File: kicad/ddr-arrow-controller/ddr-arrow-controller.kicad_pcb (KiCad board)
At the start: 2 copper layers, 50 parts

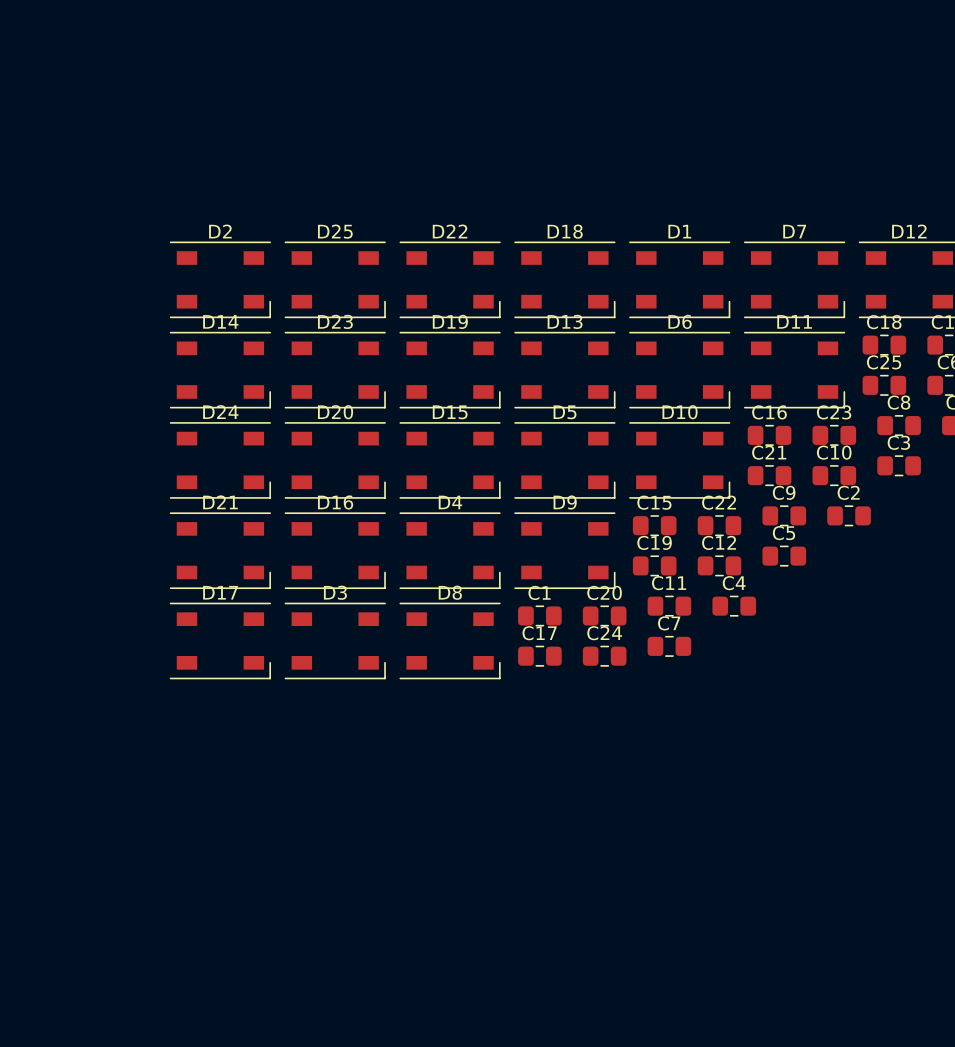
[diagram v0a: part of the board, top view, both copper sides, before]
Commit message: Schematic Updates
Placed microcontroller, CANBus chips, power regulator.
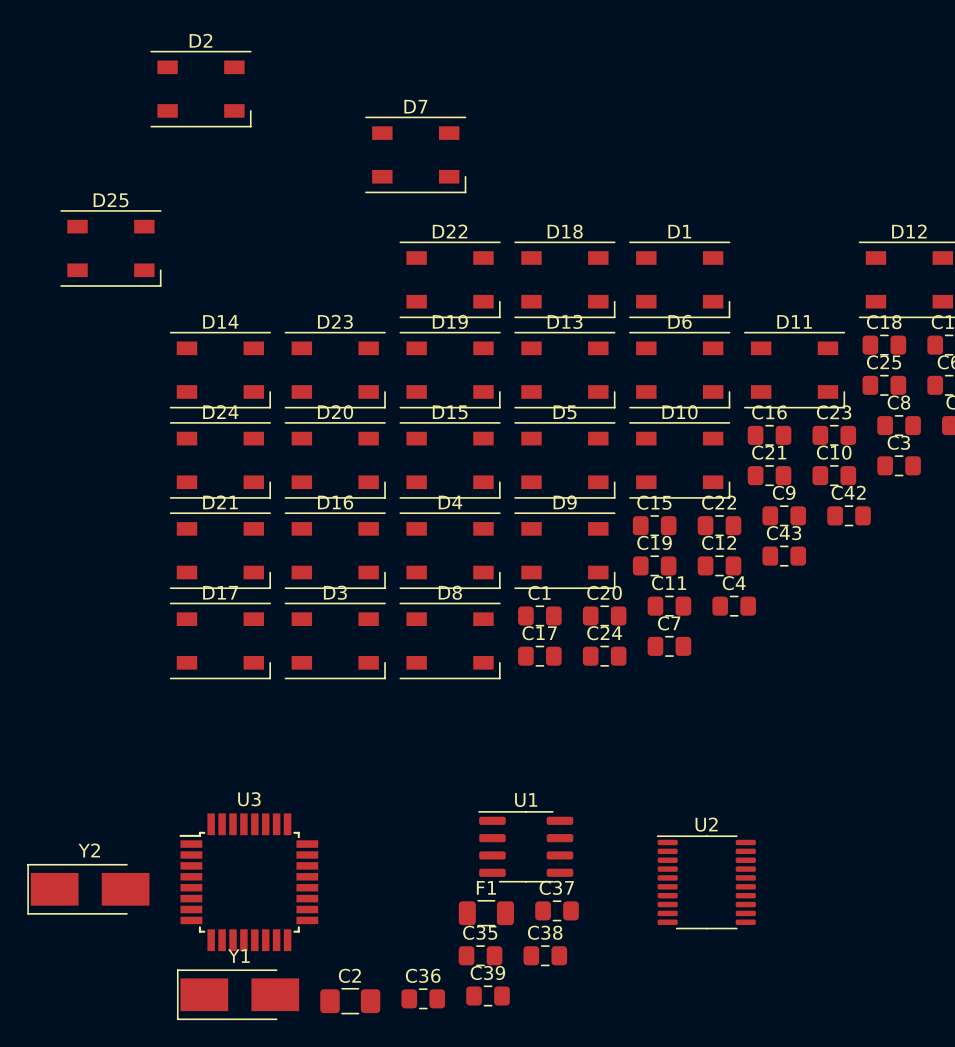
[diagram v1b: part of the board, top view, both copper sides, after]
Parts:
- added C2: 10uF, Capacitor_SMD:C_1206_3216Metric_Pad1.42x1.75mm_HandSolder, F.Cu at (36.3, 114.4)
- added C35: 1000uF, Capacitor_SMD:C_0805_2012Metric_Pad1.15x1.40mm_HandSolder, F.Cu at (45.9, 111.0)
- added C36: 1000uF, Capacitor_SMD:C_0805_2012Metric_Pad1.15x1.40mm_HandSolder, F.Cu at (41.7, 114.2)
- added C37: 1000uF, Capacitor_SMD:C_0805_2012Metric_Pad1.15x1.40mm_HandSolder, F.Cu at (51.5, 107.8)
- added C38: 1000uF, Capacitor_SMD:C_0805_2012Metric_Pad1.15x1.40mm_HandSolder, F.Cu at (50.6, 111.0)
- added C39: 1000uF, Capacitor_SMD:C_0805_2012Metric_Pad1.15x1.40mm_HandSolder, F.Cu at (46.4, 114.0)
- added F1: 1206L025YR, Fuse:Fuse_1206_3216Metric, F.Cu at (46.3, 107.9)
- added U1: TJA1051T, Package_SO:SOIC-8_3.9x4.9mm_P1.27mm, F.Cu at (49.2, 103.1)
- added U2: MCP2515-xST, Package_SO:TSSOP-20_4.4x6.5mm_P0.65mm, F.Cu at (62.5, 105.7)
- added U3: ATmega328PB-AU, Package_QFP:TQFP-32_7x7mm_P0.8mm, F.Cu at (28.9, 105.7)
- added Y1: 8MHz, Crystal:Crystal_SMD_5032-2Pin_5.0x3.2mm_HandSoldering, F.Cu at (28.2, 113.9)
- added Y2: 16MHz, Crystal:Crystal_SMD_5032-2Pin_5.0x3.2mm_HandSoldering, F.Cu at (17.3, 106.2)
- moved D7 29.2 mm to (41.1, 52.3)
- moved D25 16.6 mm to (18.8, 59.2)
- moved D2 14.1 mm to (25.4, 47.5)
- renumbered C2 to C42, C5 to C43
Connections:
- net +5V renamed VCC

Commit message: Board layout v1 complete
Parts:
- removed C36, C37, C38, C39: 1000uF, Capacitor_SMD:C_0805_2012Metric_Pad1.15x1.40mm_HandSolder
- added C26: 0.1uF, Capacitor_SMD:C_0805_2012Metric_Pad1.15x1.40mm_HandSolder, F.Cu at (152.9, 11.7)
- added C27: 0.022uF, Capacitor_SMD:C_0805_2012Metric_Pad1.15x1.40mm_HandSolder, F.Cu at (152.4, 20.3)
- added C28: 0.1uF, Capacitor_SMD:C_0805_2012Metric_Pad1.15x1.40mm_HandSolder, F.Cu at (105.2, 8.38)
- added C29: 10uF/16V, Capacitor_SMD:C_1206_3216Metric_Pad1.42x1.75mm_HandSolder, F.Cu at (105.7, 5.84)
- added C30: 22uF, Capacitor_SMD:C_0805_2012Metric_Pad1.15x1.40mm_HandSolder, F.Cu at (165.6, 21.3)
- added C31: 22uF, Capacitor_SMD:C_0805_2012Metric_Pad1.15x1.40mm_HandSolder, F.Cu at (151.9, 24.8)
- added C33: 22uF, Capacitor_SMD:C_0805_2012Metric_Pad1.15x1.40mm_HandSolder, F.Cu at (165.6, 23.9)
- added C34: 10uF, Capacitor_SMD:C_1206_3216Metric_Pad1.42x1.75mm_HandSolder, F.Cu at (165.1, 15.7)
- added C44: 0.1uF, Capacitor_SMD:C_0805_2012Metric_Pad1.15x1.40mm_HandSolder, F.Cu at (165.6, 18.8)
- added C5: 10uF/35V, Capacitor_SMD:C_1206_3216Metric_Pad1.42x1.75mm_HandSolder, F.Cu at (155.4, 11.2)
- added D26: RED, LED_SMD:LED_0805_2012Metric, F.Cu at (164.8, 40.6)
- added IC1: JanSquareLib_TS30013-M033QFNR, TS30013:QFN50P300X300X100-17N, F.Cu at (150.4, 16.3)
- added J10: OPTO, Connector_JST:JST_PH_B2B-PH-K_1x02_P2.00mm_Vertical, F.Cu at (21.8, 8.13)
- added J11: ST_POW, Connector_Molex:Molex_Mini-Fit_Jr_5569-02A2_2x01_P4.20mm_Horizontal, F.Cu at (142.7, 10.7)
- added J12: ST_CAN, TerminalBlock_Phoenix:TerminalBlock_Phoenix_MKDS-1,5-2_1x02_P5.00mm_Horizontal, F.Cu at (118.9, 5.46)
- added J13: Step Sensor, Connector_JST:JST_PH_B2B-PH-K_1x02_P2.00mm_Vertical, F.Cu at (8.64, 81.8)
- added J2: A0, Connector_JST:JST_PH_B2B-PH-K_1x02_P2.00mm_Vertical, F.Cu at (8.64, 89.0)
- added J3: A1, Connector_JST:JST_PH_B2B-PH-K_1x02_P2.00mm_Vertical, F.Cu at (162.6, 120.5)
- added J4: A2, Connector_JST:JST_PH_B2B-PH-K_1x02_P2.00mm_Vertical, F.Cu at (163.1, 51.3)
- added J5: A3, Connector_JST:JST_PH_B2B-PH-K_1x02_P2.00mm_Vertical, F.Cu at (31.2, 8.13)
- added J6: AVR-ISP-6, Connector_PinHeader_2.54mm:PinHeader_2x03_P2.54mm_Vertical, F.Cu at (73.4, 7.87)
- added JP1: LED_EN, Jumper:SolderJumper-2_P1.3mm_Bridged_Pad1.0x1.5mm, F.Cu at (157.5, 40.6)
- added JP2: Jumper_NO_Small, Connector_PinSocket_2.54mm:PinSocket_1x02_P2.54mm_Vertical, F.Cu at (113.5, 14.0)
- added L1: 4.7uH, Inductor_SMD:L_Taiyo-Yuden_NR-80xx_HandSoldering, F.Cu at (158.0, 20.3)
- added R1: 10K, Resistor_SMD:R_0805_2012Metric_Pad1.15x1.40mm_HandSolder, F.Cu at (68.4, 4.80)
- added R10: 10K, Resistor_SMD:R_0805_2012Metric_Pad1.15x1.40mm_HandSolder, F.Cu at (43.7, 34.5)
- added R11: 560, Resistor_SMD:R_0805_2012Metric_Pad1.15x1.40mm_HandSolder, F.Cu at (5.59, 71.6)
- added R12: 560, Resistor_SMD:R_0805_2012Metric_Pad1.15x1.40mm_HandSolder, F.Cu at (10.7, 71.6)
- added R13: 120, Resistor_SMD:R_0805_2012Metric_Pad1.15x1.40mm_HandSolder, F.Cu at (120.0, 14.1)
- added R2: 10K, Resistor_SMD:R_0805_2012Metric_Pad1.15x1.40mm_HandSolder, F.Cu at (105.2, 3.30)
- added R3: 560, Resistor_SMD:R_0805_2012Metric_Pad1.15x1.40mm_HandSolder, F.Cu at (18.3, 17.3)
- added R4: 1K, Resistor_SMD:R_0805_2012Metric_Pad1.15x1.40mm_HandSolder, F.Cu at (23.4, 17.3)
- added R5: 1K, Resistor_SMD:R_0805_2012Metric_Pad1.15x1.40mm_HandSolder, F.Cu at (161.0, 41.4)
- added R6: 10K, Resistor_SMD:R_0805_2012Metric_Pad1.15x1.40mm_HandSolder, F.Cu at (40.6, 34.5)
- added R7: 10K, Resistor_SMD:R_0805_2012Metric_Pad1.15x1.40mm_HandSolder, F.Cu at (38.1, 34.5)
- added R8: 10K, Resistor_SMD:R_0805_2012Metric_Pad1.15x1.40mm_HandSolder, F.Cu at (35.6, 34.5)
- added R9: 470, Resistor_SMD:R_0805_2012Metric_Pad1.15x1.40mm_HandSolder, F.Cu at (25.9, 21.3)
- added REF**: OSHW-Logo2_14.6x12mm_SilkScreen, Symbol:OSHW-Logo2_14.6x12mm_SilkScreen, F.Cu at (135.6, 159.3)
- added REF**: MountingHole_4.3mm_M4_DIN965_Pad, MountingHole:MountingHole_4.3mm_M4_DIN965_Pad, F.Cu at (166.0, 166.0)
- added REF**: MountingHole_4.3mm_M4_DIN965_Pad, MountingHole:MountingHole_4.3mm_M4_DIN965_Pad, F.Cu at (6.00, 166.0)
- added REF**: MountingHole_4.3mm_M4_DIN965_Pad, MountingHole:MountingHole_4.3mm_M4_DIN965_Pad, F.Cu at (6.00, 6.00)
- added REF**: MountingHole_4.3mm_M4_DIN965_Pad, MountingHole:MountingHole_4.3mm_M4_DIN965_Pad, F.Cu at (166.0, 6.00)
- added SW1: SW_Push, Button_Switch_SMD:SW_SPST_CK_RS282G05A3, F.Cu at (42.4, 6.86)
- added SW2: SW_DIP_x04, Button_Switch_SMD:SW_DIP_SPSTx04_Slide_9.78x12.34mm_W8.61mm_P2.54mm, F.Cu at (39.6, 43.7)
- added TP1: TP_PG, TestPoint:TestPoint_Pad_1.0x1.0mm, F.Cu at (148.5, 20.8)
- added TP10: PC5, TestPoint:TestPoint_Pad_1.0x1.0mm, B.Cu at (49.0, 11.7)
- added TP11: 5V, TestPoint:TestPoint_Pad_D2.0mm, B.Cu at (74.5, 18.2)
- added TP12: GND, TestPoint:TestPoint_Pad_D2.0mm, B.Cu at (71.5, 18.2)
- added TP13: PD0, TestPoint:TestPoint_Pad_D2.0mm, B.Cu at (65.3, 18.2)
- added TP14: PD1, TestPoint:TestPoint_Pad_D2.0mm, B.Cu at (68.4, 18.2)
- added TP2: TP_EN, TestPoint:TestPoint_Pad_1.0x1.0mm, F.Cu at (150.6, 22.0)
- added TP3: PE2, TestPoint:TestPoint_Pad_1.0x1.0mm, F.Cu at (72.4, 4.57)
- added TP4: PE3, TestPoint:TestPoint_Pad_1.0x1.0mm, F.Cu at (35.7, 3.40)
- added TP5: PB1, TestPoint:TestPoint_Pad_D2.0mm, F.Cu at (68.4, 16.6)
- added TP6: PB0, TestPoint:TestPoint_Pad_D2.0mm, F.Cu at (65.4, 16.6)
- added TP7: PE1, TestPoint:TestPoint_Pad_1.0x1.0mm, B.Cu at (64.2, 10.9)
- added TP8: PC4, TestPoint:TestPoint_Pad_1.0x1.0mm, B.Cu at (51.3, 11.6)
- added U4: TLP290, Package_SO:SOP-4_4.4x2.6mm_P1.27mm, F.Cu at (20.8, 14.2)
- added U5: TLP290, Package_SO:SOP-4_4.4x2.6mm_P1.27mm, F.Cu at (8.13, 75.2)
- C2: value 10uF -> 0.1uF; footprint Capacitor_SMD:C_1206_3216Metric_Pad1.42x1.75mm_HandSolder -> Capacitor_SMD:C_0805_2012Metric_Pad1.15x1.40mm_HandSolder
- C35: footprint Capacitor_SMD:C_0805_2012Metric_Pad1.15x1.40mm_HandSolder -> Capacitor_SMD:C_Elec_10x10.2
- U2: value MCP2515-xST -> MCP2515-xSO; footprint Package_SO:TSSOP-20_4.4x6.5mm_P0.65mm -> Package_SO:SOIC-18W_7.5x11.6mm_P1.27mm
- Y1: value 8MHz -> 16MHz; footprint Crystal:Crystal_SMD_5032-2Pin_5.0x3.2mm_HandSoldering -> Crystal:Resonator_SMD_muRata_CSTxExxV-3Pin_3.0x1.1mm_HandSoldering
- Y2: value 16MHz -> 8MHz; footprint Crystal:Crystal_SMD_5032-2Pin_5.0x3.2mm_HandSoldering -> Crystal:Resonator_SMD_muRata_CSTxExxV-3Pin_3.0x1.1mm_HandSoldering
- moved D25 153.7 mm to (145.8, 145.8), turned to 90 degrees
- moved C35 139.1 mm to (161.0, 33.0)
- moved Y2 129.0 mm to (99.6, 6.86), turned to 270 degrees
- moved D16 115.8 mm to (145.8, 115.8), turned to 270 degrees
- moved C2 115.3 mm to (63.2, 2.29), turned to 180 degrees
- moved D24 113.9 mm to (115.8, 145.8), turned to 90 degrees
- moved D5 105.7 mm to (145.9, 26.0), turned to 90 degrees
- moved C25 105.6 mm to (149.6, 144.4), turned to 270 degrees
- moved U1 104.6 mm to (105.2, 14.6)
- moved D15 102.7 mm to (145.8, 85.9), turned to 90 degrees
- moved U2 99.0 mm to (90.2, 10.7), turned to 180 degrees
- moved U3 98.9 mm to (56.4, 10.7), turned to 45 degrees
- moved Y1 98.6 mm to (52.3, 18.3), turned to 315 degrees
- moved C24 97.9 mm to (149.6, 114.4), turned to 270 degrees
- moved C21 97.3 mm to (149.9, 24.8), turned to 270 degrees
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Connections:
- C1 pad 1: VCC -> AVR_V
- C10 pad 1: VCC -> AVR_V
- C11 pad 1: VCC -> AVR_V
- C12 pad 1: VCC -> AVR_V
- C13 pad 1: VCC -> AVR_V
- C14 pad 1: VCC -> AVR_V
- C15 pad 1: VCC -> AVR_V
- C16 pad 1: VCC -> AVR_V
- C17 pad 1: VCC -> AVR_V
- C18 pad 1: VCC -> AVR_V
- C19 pad 1: VCC -> AVR_V
- C2 pad 1: VCC -> Net-(C2-Pad1)
- C20 pad 1: VCC -> AVR_V
- C21 pad 1: VCC -> AVR_V
- C22 pad 1: VCC -> AVR_V
- C23 pad 1: VCC -> AVR_V
- C24 pad 1: VCC -> AVR_V
- C25 pad 1: VCC -> AVR_V
- C3 pad 1: VCC -> AVR_V
- C35 pad 1: VCC -> AVR_V
- C4 pad 1: VCC -> AVR_V
- C42 pad 1: VCC -> AVR_V
- C43 pad 1: VCC -> AVR_V
- C6 pad 1: VCC -> AVR_V
- C7 pad 1: VCC -> AVR_V
- C8 pad 1: VCC -> AVR_V
- C9 pad 1: VCC -> AVR_V
- D1 pad 1: VCC -> AVR_V
- D10 pad 1: VCC -> GND
- D10 pad 3: GND -> AVR_V
- D11 pad 1: VCC -> AVR_V
- D11 pad 2: Net-(D11-Pad2) -> Net-(D10-Pad4)
- D12 pad 1: GND -> AVR_V
- D12 pad 2: Net-(D12-Pad2) -> Net-(D11-Pad4)
- D12 pad 3: VCC -> GND
- D13 pad 1: VCC -> AVR_V
- D13 pad 2: Net-(D13-Pad2) -> Net-(D12-Pad4)
- D14 pad 1: GND -> AVR_V
- D14 pad 2: Net-(D14-Pad2) -> Net-(D13-Pad4)
- D14 pad 3: VCC -> GND
- D15 pad 1: VCC -> AVR_V
- D15 pad 2: Net-(D10-Pad4) -> Net-(D14-Pad4)
- D16 pad 1: VCC -> GND
- D16 pad 2: Net-(D11-Pad4) -> Net-(D15-Pad4)
- D16 pad 3: GND -> AVR_V
- D17 pad 2: Net-(D17-Pad2) -> Net-(D16-Pad4)
- D17 pad 3: VCC -> AVR_V
- D17 pad 4: Net-(D12-Pad2) -> Net-(D17-Pad4)
- D18 pad 1: VCC -> GND
- D18 pad 2: Net-(D13-Pad4) -> Net-(D17-Pad4)
- D18 pad 3: GND -> AVR_V
- D19 pad 2: Net-(D19-Pad2) -> Net-(D18-Pad4)
- D19 pad 3: VCC -> AVR_V
- D19 pad 4: Net-(D14-Pad2) -> Net-(D19-Pad4)
- D2 pad 1: GND -> AVR_V
- D2 pad 2: Net-(D2-Pad2) -> Net-(D1-Pad4)
- D2 pad 3: VCC -> GND
- D20 pad 1: VCC -> GND
- D20 pad 2: Net-(D15-Pad4) -> Net-(D19-Pad4)
- D20 pad 3: GND -> AVR_V
- D21 pad 1: VCC -> AVR_V
- D21 pad 2: Net-(D16-Pad4) -> Net-(D20-Pad4)
- D22 pad 1: GND -> AVR_V
- D22 pad 3: VCC -> GND
- D22 pad 4: Net-(D17-Pad2) -> Net-(D22-Pad4)
- D23 pad 1: VCC -> AVR_V
- D23 pad 2: Net-(D18-Pad4) -> Net-(D22-Pad4)
- D24 pad 1: GND -> AVR_V
- D24 pad 3: VCC -> GND
- D24 pad 4: Net-(D19-Pad2) -> Net-(D24-Pad4)
- D25 pad 1: VCC -> AVR_V
- D25 pad 2: Net-(D20-Pad4) -> Net-(D24-Pad4)
- D3 pad 1: VCC -> AVR_V
- D4 pad 1: GND -> AVR_V
- D4 pad 2: Net-(D4-Pad2) -> Net-(D3-Pad4)
- D4 pad 3: VCC -> GND
- D5 pad 1: VCC -> AVR_V
- D5 pad 4: Net-(D10-Pad2) -> Net-(D5-Pad4)
- D6 pad 1: VCC -> GND
- D6 pad 2: Net-(D1-Pad4) -> Net-(D5-Pad4)
- D6 pad 3: GND -> AVR_V
- D6 pad 4: Net-(D11-Pad2) -> Net-(D6-Pad4)
- D7 pad 2: Net-(D12-Pad4) -> Net-(D6-Pad4)
- D7 pad 3: VCC -> AVR_V
- D7 pad 4: Net-(D2-Pad2) -> Net-(D7-Pad4)
- D8 pad 1: VCC -> GND
- D8 pad 2: Net-(D3-Pad4) -> Net-(D7-Pad4)
- D8 pad 3: GND -> AVR_V
- D8 pad 4: Net-(D13-Pad2) -> Net-(D8-Pad4)
- D9 pad 2: Net-(D14-Pad4) -> Net-(D8-Pad4)
- D9 pad 3: VCC -> AVR_V
- D9 pad 4: Net-(D4-Pad2) -> Net-(D10-Pad2)
- F1 pad 1: Net-(F1-Pad1) -> AVR_V
- F1 pad 2: VCC -> AVR_V
- U1 pad 3: VCC -> AVR_V
- U2 pad 10: GND -> Net-(U2-Pad10)
- U2 pad 13: Net-(U2-Pad13) -> PB5
- U2 pad 14: PB5 -> PB3
- U2 pad 15: Net-(U2-Pad15) -> PB4
- U2 pad 16: PB3 -> PB2
- U2 pad 17: PB4 -> Net-(R2-Pad1)
- U2 pad 18: PB2 -> AVR_V
- U2 pad 8: Net-(C40-Pad2) -> Net-(U2-Pad8)
- U2 pad 9: Net-(C41-Pad2) -> GND
- U3 pad 18: Net-(F1-Pad1) -> AVR_V
- U3 pad 19: Net-(U3-Pad19) -> PE2
- U3 pad 20: Net-(C27-Pad1) -> Net-(C2-Pad1)
- U3 pad 22: Net-(U3-Pad22) -> PE3
- U3 pad 3: Net-(U3-Pad3) -> PE0
- U3 pad 4: Net-(F1-Pad1) -> AVR_V
- U3 pad 6: Net-(U3-Pad6) -> PE1
- U3 pad 7: Net-(C32-Pad2) -> Net-(U3-Pad7)
- U3 pad 8: Net-(C31-Pad2) -> Net-(U3-Pad8)
- Y1 pad 1: Net-(C40-Pad2) -> Net-(U3-Pad7)
- Y1 pad 2: Net-(C41-Pad2) -> GND
- Y2 pad 1: Net-(C31-Pad2) -> Net-(U2-Pad8)
- Y2 pad 2: Net-(C32-Pad2) -> GND
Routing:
- net AVR_V: track 0.00 -> 1074.3 mm, vias 0 -> 3
- net GND: track 0.00 -> 1010.5 mm, vias 0 -> 31
- net PC1: track 0.00 -> 276.7 mm, vias 0 -> 1
- net PC2: track 0.00 -> 203.4 mm, vias 0 -> 1
- net PC0: track 0.00 -> 126.0 mm, vias 0 -> 2
- net PE0: track 0.00 -> 94.4 mm, vias 0 -> 2
- net PD4: track 0.00 -> 57.0 mm, vias 0 -> 2
- net PD3: track 0.00 -> 56.8 mm, vias 0 -> 2
- net PD7: track 0.00 -> 54.3 mm
- net PD5: track 0.00 -> 37.5 mm, vias 0 -> 2
- net Net-(D15-Pad4): track 0.00 -> 36.5 mm
- net PD6: track 0.00 -> 36.2 mm, vias 0 -> 2
- net Net-(D5-Pad4): track 0.00 -> 33.6 mm
- net Net-(D10-Pad4): track 0.00 -> 32.3 mm
- net PE3: track 0.00 -> 31.7 mm
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- added copper zone on B.Cu, net GND
- added copper zone on F.Cu, net GND
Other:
- board outline added: 172 x 172 mm
- rule pad_to_mask_clearance: 0.05 -> 0
- board text added: "+"
- board text added: "-"
- board text added: "5V"
- board text added: "CAN Terminator"
- board text added: "CAN-L"
- board text added: "FSR"
- board text added: "Gnd"
- board text added: "Light IN"
- board text added: "MISO VCC"
- board text added: "RST GND"
- board text added: "Reset"
- board text added: "Rx"
- board text added: "SCK MOSI"
- board text added: "Sean Starnes - 2020 Arrow Controller http://starn.es"
- board text added: "Step OUT"
- board text added: "Tx"
- board text added: "X0XX: Player XX00: Arrow 0XXX: Mode"
